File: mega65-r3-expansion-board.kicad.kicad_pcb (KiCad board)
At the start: 4 copper layers, 215 x 126.9 mm, 99 parts, among them J1 Conn_01x04, J10 PMOD2, J11 Conn_02x05_Odd_Even, J12 Conn_02x17_Odd_Even, J13 Conn_02x17_Odd_Even, J14 Component A/V, J15 ESP32 Connector, J2 Conn_01x04, J3 C64_User_Port, J4 Mini-DIN-8-With-Shield, J5 C64_Tape_Port, J6 OKR-T/3-W12-C, J7 Conn_02x06_Odd_Even, J8 Conn_02x06_Odd_Even, J9 PMOD1, U1 74HC595, U10 74LS125, U11 74HC595, U12 74LS125, U13 74LS125, U2 74LVC165, U3 74LS125, U4 74HC595, U5 74LVC165, U6 74HC595, U7 74LVC165, U8 74LS125, U9 74LS125

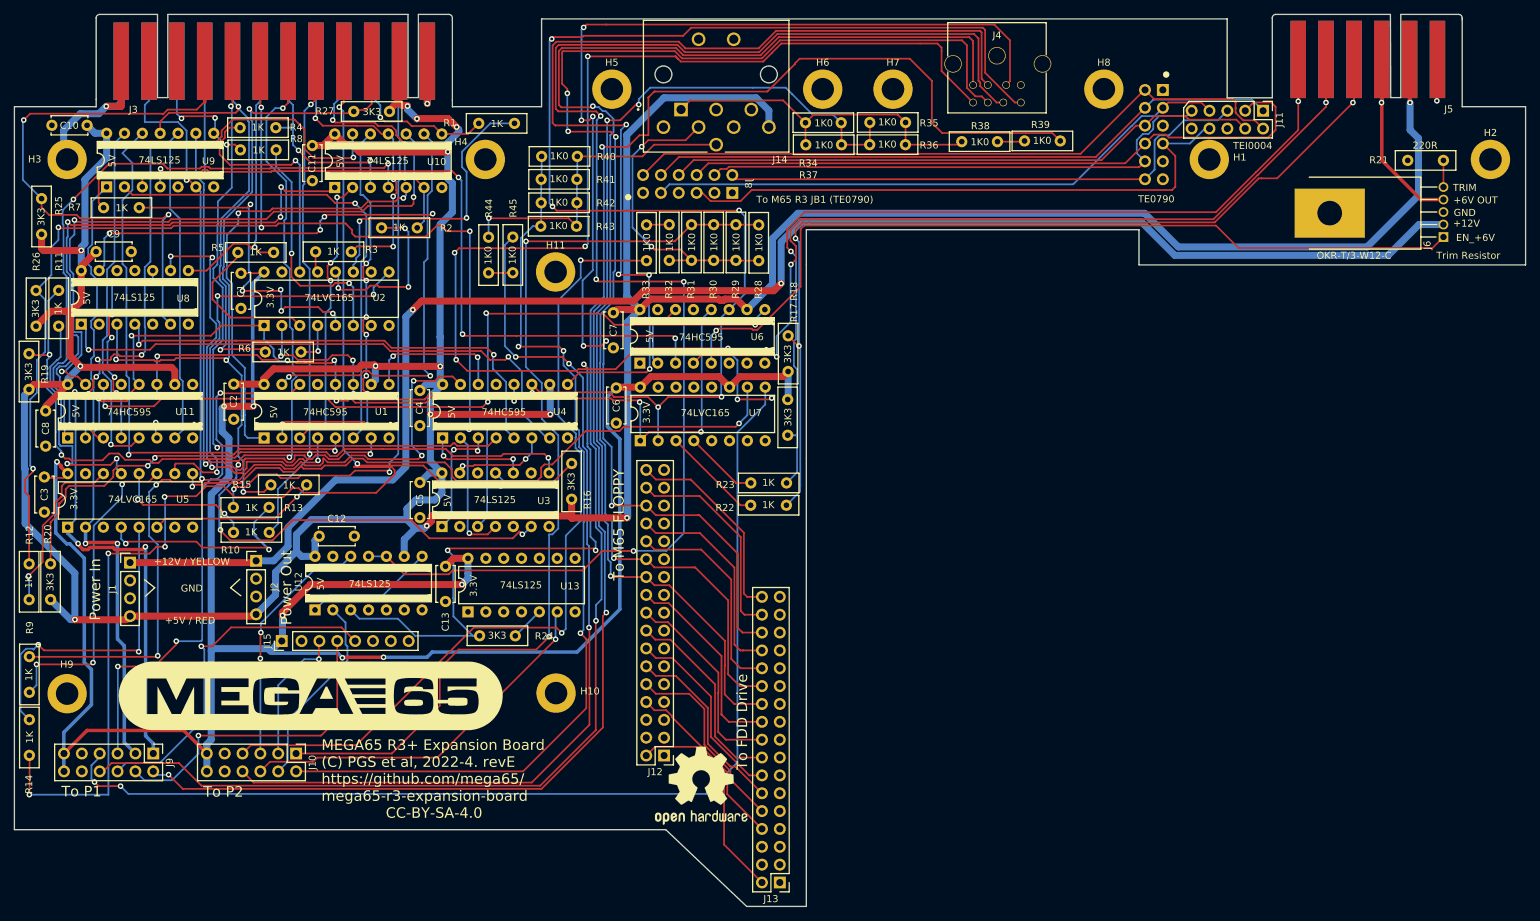
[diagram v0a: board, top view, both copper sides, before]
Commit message: reroute 1565 clock, LD and 5V WIFI_EN line
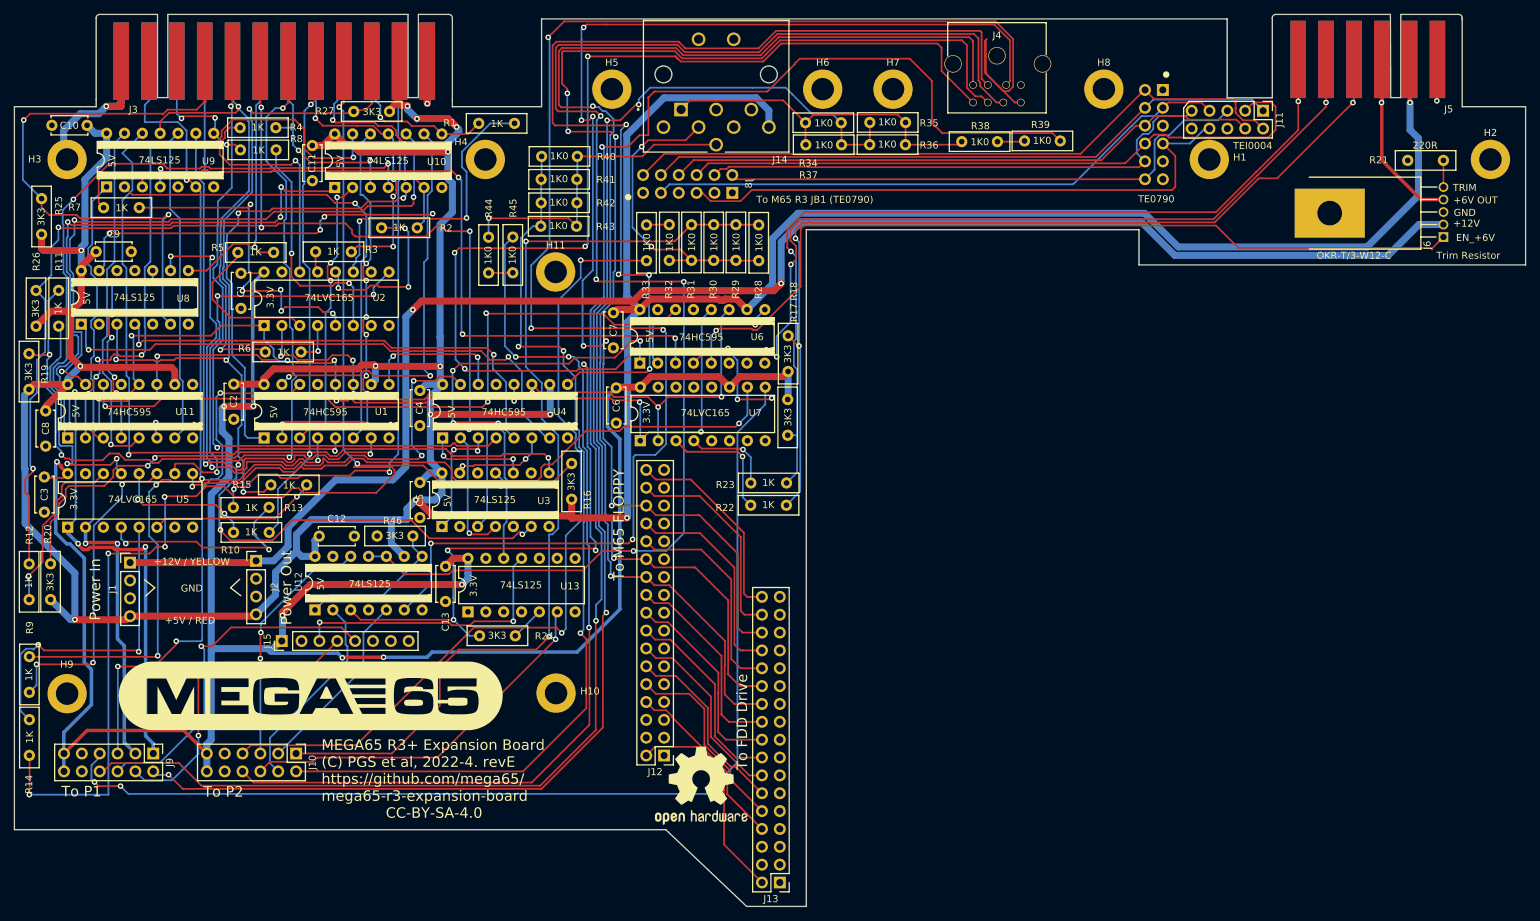
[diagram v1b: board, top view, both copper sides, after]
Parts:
- added R46: 3K3, snapeda:Labeled Resistor, F.Cu at (70.4, 101.3)
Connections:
- net 1565_LD renamed 1565_LD_5V
- net 1565_SERIO renamed /C1565 External C65 Drive Port/SERIO_5V
- net EN_1565_SERIO renamed Net-(R46-Pad2)
- J10 pad 3: WIFI_EN -> 1565_CLOCK_3V3
- J15 pad 3: WIFI_EN -> WIFI_EN_3V3
- J4 pad 8: EXP_CLOCK -> Net-(J4-Pad8)
- U12 pad 4: unconnected-(U12-Pad4) -> GND
- U12 pad 5: unconnected-(U12-Pad5) -> 1565_CLOCK_3V3
- U12 pad 6: unconnected-(U12-Pad6) -> Net-(J4-Pad8)
- U13 pad 11: unconnected-(U13-Pad11) -> WIFI_EN_3V3
- U13 pad 12: unconnected-(U13-Pad12) -> WIFI_EN_5V
- U13 pad 13: unconnected-(U13-Pad13) -> GND
- U6 pad 1: unconnected-(U6-QB-Pad1) -> WIFI_EN_5V
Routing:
- net Net-(J4-Pad8): track 0.00 -> 231.7 mm, vias 0 -> 5
- net EXP_CLOCK: track 326.2 -> 184.5 mm, vias 14 -> 11
- net WIFI_EN_5V: track 0.00 -> 65.5 mm, vias 0 -> 4
- net WIFI_EN_3V3: track 0.00 -> 40.2 mm, vias 0 -> 2
- net 1565_CLOCK_3V3: track 0.00 -> 26.8 mm
- net WIFI_EN: track 19.7 -> 0.00 mm, vias 1 -> 0
- net /C1565 External C65 Drive Port/SERIO_5V: track 261.7 -> 257.0 mm, vias 10 -> 11
- net Net-(R46-Pad2): track 18.4 -> 21.8 mm
- net Net-(U7-D4): track 14.4 -> 17.5 mm, vias 0 -> 1
- net Net-(U7-D5): track 10.6 -> 12.9 mm, vias 0 -> 1
- net COMP_CHROMA2: track 132.1 -> 133.3 mm
- net 1565_SERIO_O: track 27.9 -> 28.9 mm
- net +5V: track 625.4 -> 624.7 mm
- net UART_RX: track 45.5 -> 44.9 mm

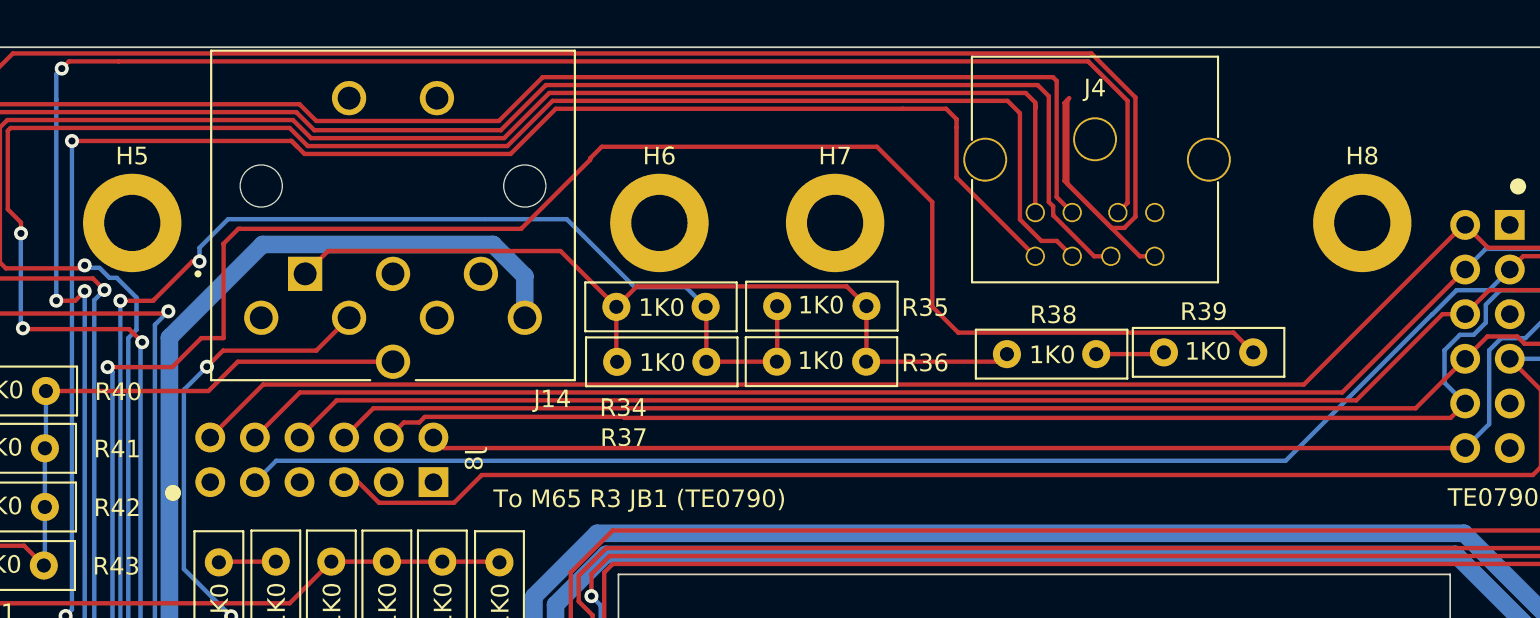
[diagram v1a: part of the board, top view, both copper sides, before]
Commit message: add A/V filter circuits and audio links to bridge board
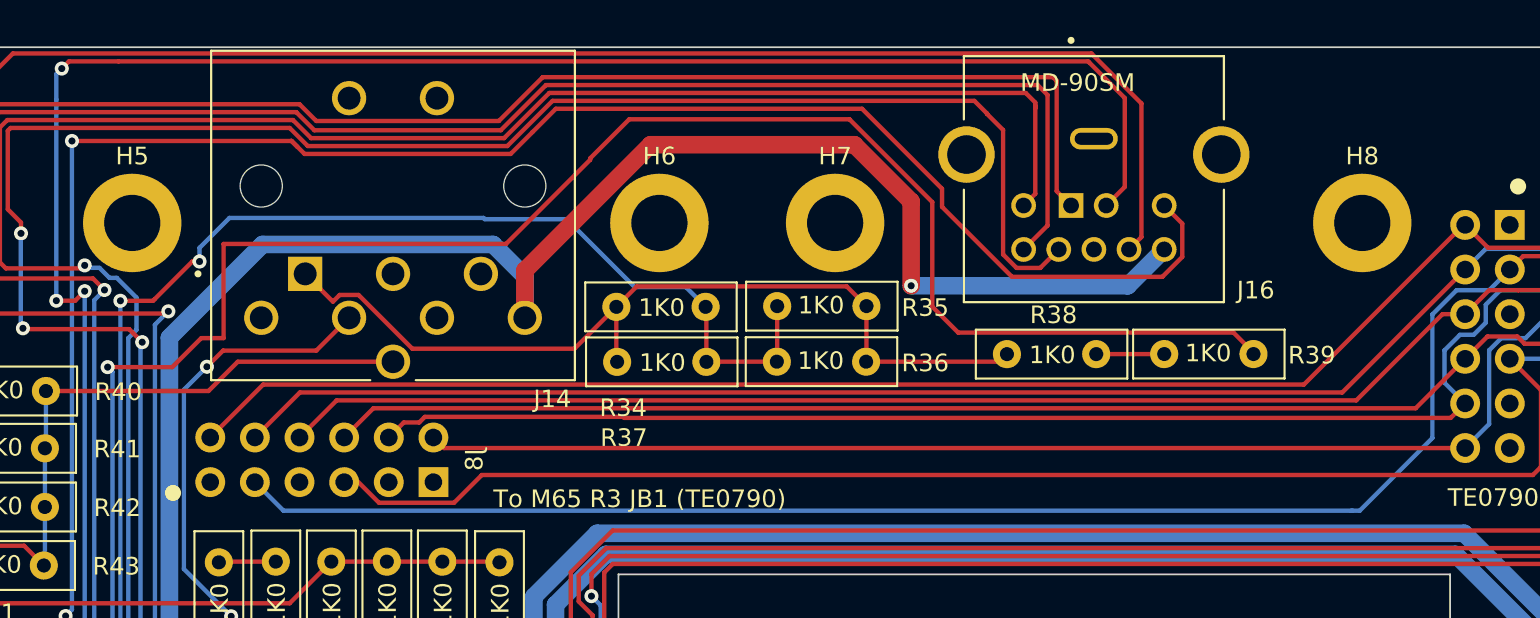
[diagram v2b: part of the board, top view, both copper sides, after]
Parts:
- removed J4: Mini-DIN-8-With-Shield, snapeda:mini-DIN-8
- added J16: MD-90SM, snapeda:CUI_MD-90SM, F.Cu at (158.6, 32.9)
- moved R39 0.10 mm to (162.6, 45.2)
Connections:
- U12 pad 6: Net-(J4-Pad8) -> /C1565 External C65 Drive Port/CLOCK_5V
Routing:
- net Net-(J4-Pad8): track 231.7 -> 0.00 mm, vias 5 -> 0
- net /C1565 External C65 Drive Port/CLOCK_5V: track 0.00 -> 212.2 mm, vias 0 -> 5
- net +5V: track 624.7 -> 673.8 mm, vias 14 -> 15
- net /C1565 External C65 Drive Port/SERIO_5V: track 257.0 -> 268.3 mm
- net /Multiplexor Interconnect Bus/TE0790_3: track 83.9 -> 89.4 mm
- net 1565_LD_5V: track 208.9 -> 207.1 mm
- net COMP_COMP2: track 242.0 -> 243.2 mm
- net /Composite and component video output/COMP_COMP: track 49.3 -> 50.5 mm
- net FL_WGATE: track 184.5 -> 185.1 mm

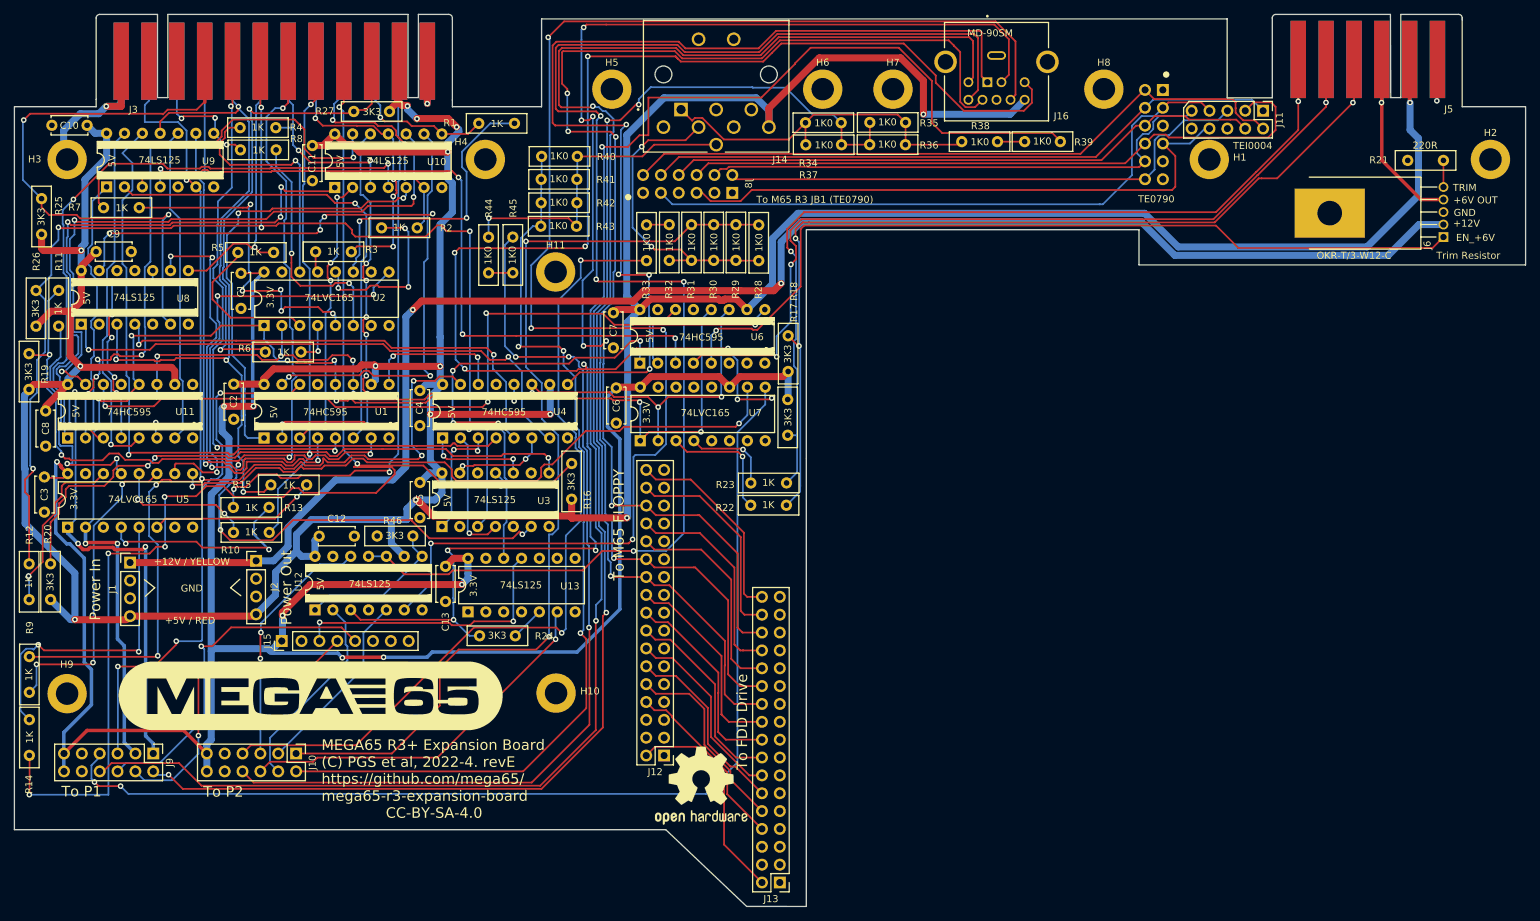
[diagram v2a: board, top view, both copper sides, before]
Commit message: route filters for other video channels
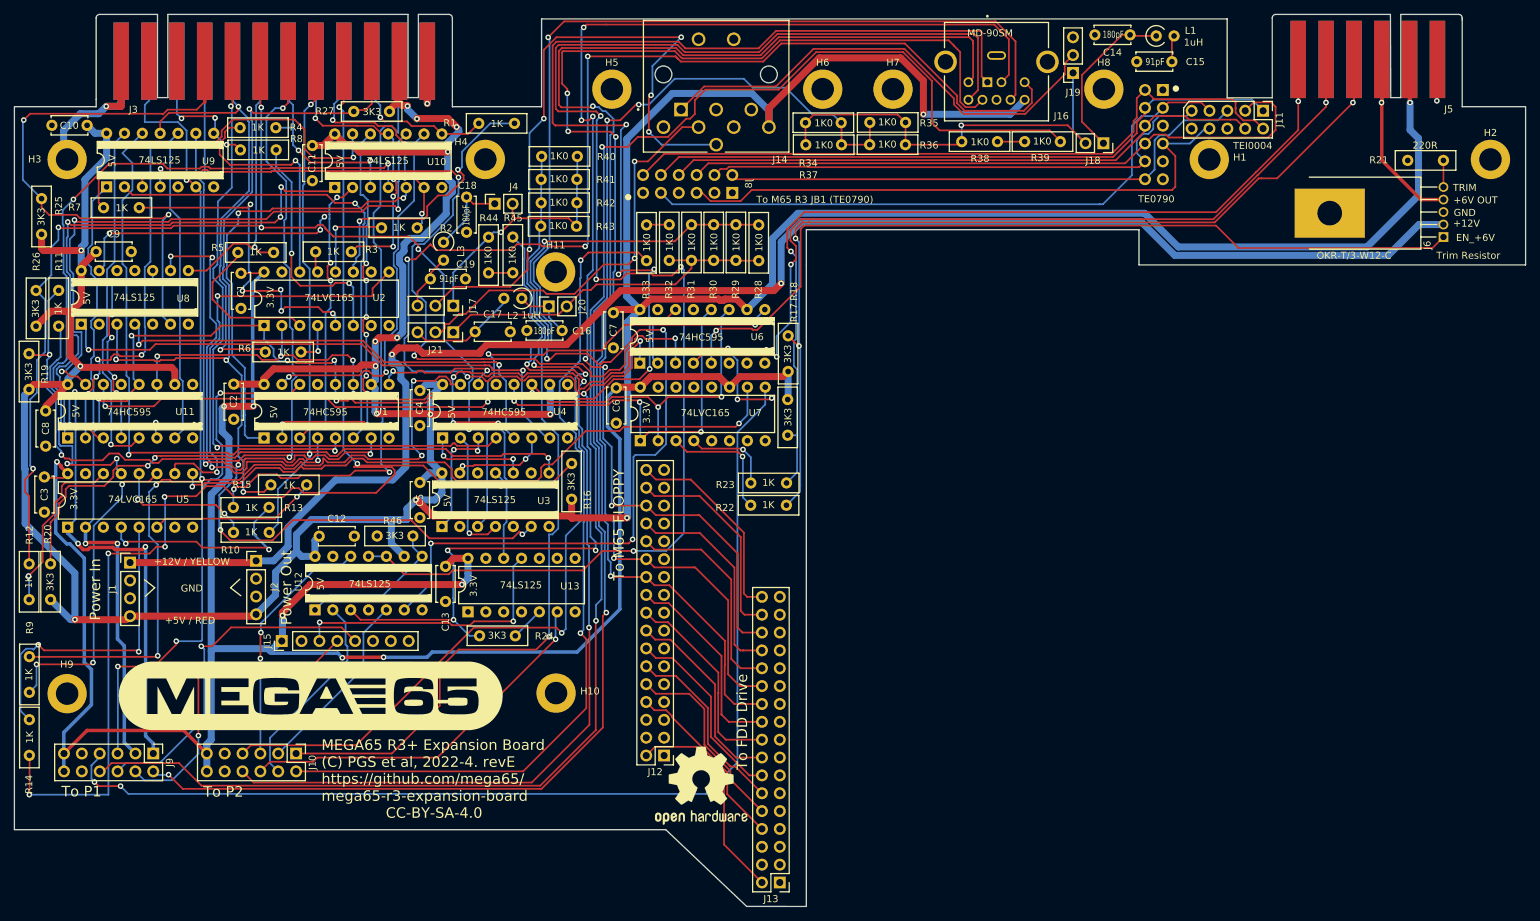
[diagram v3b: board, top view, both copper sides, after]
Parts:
- added C14: 180pF, Capacitor_THT:C_Disc_D5.0mm_W2.5mm_P5.00mm, F.Cu at (177.6, 30.0)
- added C15: 91pF, Capacitor_THT:C_Disc_D5.0mm_W2.5mm_P5.00mm, F.Cu at (183.5, 33.8)
- added C16: 180pF, Capacitor_THT:C_Disc_D5.0mm_W2.5mm_P5.00mm, F.Cu at (96.7, 72.1)
- added C17: 91pF, Capacitor_THT:C_Disc_D5.0mm_W2.5mm_P5.00mm, F.Cu at (84.4, 72.2)
- added C18: 180pF, Capacitor_THT:C_Disc_D5.0mm_W2.5mm_P5.00mm, F.Cu at (83.2, 53.1)
- added C19: 91pF, Capacitor_THT:C_Disc_D5.0mm_W2.5mm_P5.00mm, F.Cu at (78.0, 64.7)
- added J17: Conn_01x03, Connector_PinSocket_2.54mm:PinSocket_1x03_P2.54mm_Vertical, F.Cu at (81.3, 68.5)
- added J18: Conn_01x02, Connector_PinSocket_2.54mm:PinSocket_1x02_P2.54mm_Vertical, F.Cu at (173.8, 45.4)
- added J19: Conn_01x03, Connector_PinSocket_2.54mm:PinSocket_1x03_P2.54mm_Vertical, F.Cu at (169.4, 35.4)
- added J20: Conn_01x02, Connector_PinSocket_2.54mm:PinSocket_1x02_P2.54mm_Vertical, F.Cu at (94.9, 68.6)
- added J21: Conn_01x03, Connector_PinSocket_2.54mm:PinSocket_1x03_P2.54mm_Vertical, F.Cu at (81.3, 72.3)
- added J4: Conn_01x02, Connector_PinSocket_2.54mm:PinSocket_1x02_P2.54mm_Vertical, F.Cu at (87.2, 54.0)
- added L1: 1uH, Inductor_THT:L_Axial_L6.6mm_D2.7mm_P2.54mm_Vertical_Vishay_IM-2, F.Cu at (181.3, 30.1)
- added L2: 1uH, Inductor_THT:L_Axial_L6.6mm_D2.7mm_P2.54mm_Vertical_Vishay_IM-2, F.Cu at (91.0, 67.5)
- added L3: 1uH, Inductor_THT:L_Axial_L6.6mm_D2.7mm_P2.54mm_Vertical_Vishay_IM-2, F.Cu at (79.9, 59.5)
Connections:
- J14 pad 1: /Composite and component video output/COMP_COMP -> /Composite and component video output/COMPOSITE_OUT
- J14 pad 3: /Composite and component video output/AUDIO_R -> AUDIO_OUT_R
- J14 pad 4: /Composite and component video output/COMP_LUMA -> /Composite and component video output/LUMA_OUT
- J14 pad 5: unconnected-(J14-Pad5) -> AUDIO_OUT_L
- J14 pad 6: /Composite and component video output/COMP_CHROMA -> /Composite and component video output/CHROMA_OUT
- J15 pad 7: unconnected-(J15-Pin_7-Pad7) -> AUDIO_OUT_R
- J15 pad 8: unconnected-(J15-Pin_8-Pad8) -> AUDIO_OUT_L
- R28 pad 2: /Composite and component video output/COMP_LUMA -> /Composite and component video output/LUMA_UNFILTERED
- R29 pad 2: /Composite and component video output/COMP_LUMA -> /Composite and component video output/LUMA_UNFILTERED
- R30 pad 2: /Composite and component video output/COMP_LUMA -> /Composite and component video output/LUMA_UNFILTERED
- R31 pad 2: /Composite and component video output/COMP_LUMA -> /Composite and component video output/LUMA_UNFILTERED
- R32 pad 2: /Composite and component video output/COMP_LUMA -> /Composite and component video output/LUMA_UNFILTERED
- R34 pad 2: /Composite and component video output/COMP_COMP -> /Composite and component video output/COMPOSITE_UNFILTERED
- R35 pad 2: /Composite and component video output/COMP_COMP -> /Composite and component video output/COMPOSITE_UNFILTERED
- R36 pad 2: /Composite and component video output/COMP_COMP -> /Composite and component video output/COMPOSITE_UNFILTERED
- R37 pad 2: /Composite and component video output/COMP_COMP -> /Composite and component video output/COMPOSITE_UNFILTERED
- R38 pad 2: /Composite and component video output/COMP_COMP -> /Composite and component video output/COMPOSITE_UNFILTERED
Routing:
- net /Composite and component video output/CHROMA_OUT: track 0.00 -> 93.5 mm, vias 0 -> 5
- net /Composite and component video output/COMPOSITE_OUT: track 0.00 -> 68.1 mm
- net /Composite and component video output/COMPOSITE_UNFILTERED: track 0.00 -> 61.5 mm, vias 0 -> 1
- net /Composite and component video output/LUMA_OUT: track 0.00 -> 58.4 mm, vias 0 -> 2
- net /Composite and component video output/LUMA_UNFILTERED: track 0.00 -> 51.5 mm
- net /Composite and component video output/COMP_COMP: track 50.5 -> 0.00 mm
- net /Composite and component video output/COMP_LUMA: track 44.4 -> 0.00 mm, vias 2 -> 0
- net Net-(J18-Pin_1): track 0.00 -> 24.0 mm
- net /User Port & Tape Port/EN_PA2: track 102.4 -> 122.4 mm
- net /Composite and component video output/LUMA_FILTERED: track 0.00 -> 15.6 mm
- net /C1565 External C65 Drive Port/SERIO_5V: track 268.3 -> 283.8 mm
- net unconnected-(U8-Pad13): track 53.8 -> 38.6 mm, vias 4 -> 3
- net Net-(J4-Pin_1): track 0.00 -> 12.2 mm
- net Net-(U2-D1): track 24.9 -> 13.0 mm, vias 3 -> 1
- net Net-(J20-Pin_1): track 0.00 -> 8.53 mm
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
